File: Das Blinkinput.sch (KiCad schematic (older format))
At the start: 10 parts

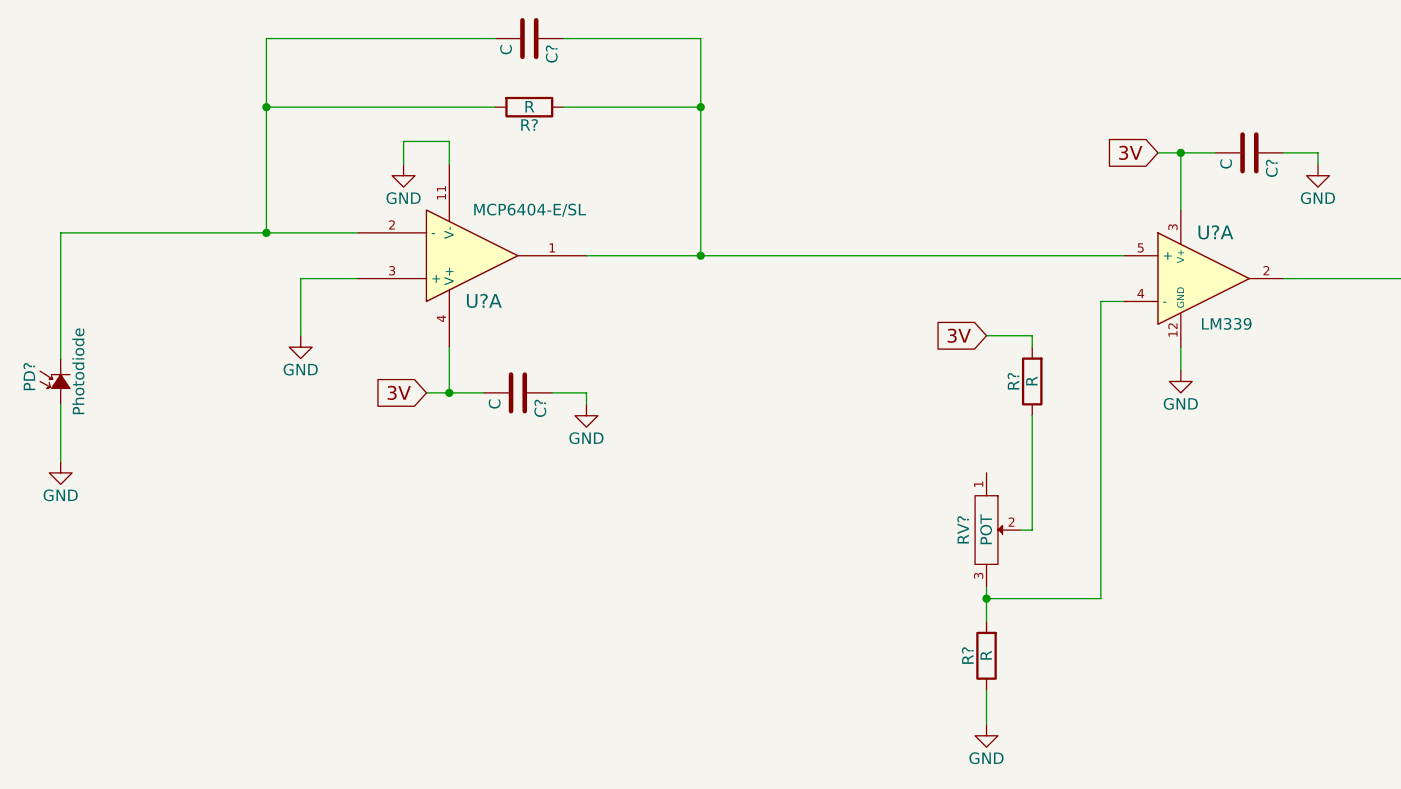
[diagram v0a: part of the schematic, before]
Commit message: Added part numbers and links to schematic
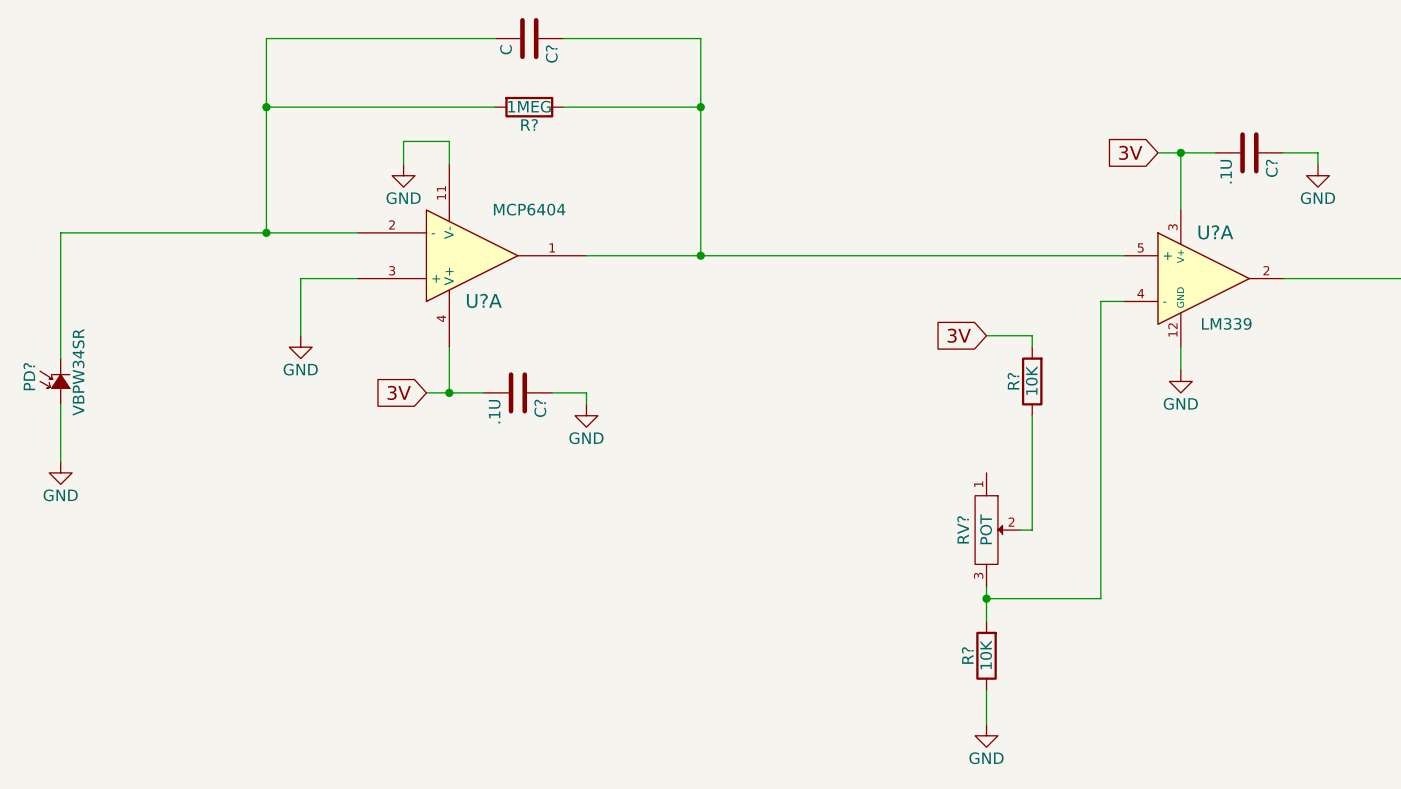
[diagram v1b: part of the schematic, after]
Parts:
- C? (x2): value C -> .1U
- PD?: value Photodiode -> VBPW34SR; Link (none) -> http://parts.io/detail/2942714/VBPW34SR; MPN (none) -> VBPW34SR
- R?: value R -> 1MEG; Link (none) -> http://parts.io/detail/880921/RC1206FR-071ML; MPN (none) -> RC1206FR-071ML
- R? (x2): value R -> 10K
- RV?: MPN (none) -> P090L-02F25BR10K
- U?: value MCP6404-E/SL -> MCP6404; Link (none) -> http://parts.io/detail/3584122/MCP6404-E%2FSL; MPN (none) -> MCP6404-E/SL
- U?: Link (none) -> http://parts.io/detail/916254/LM339DE4; MPN (none) -> LM339DE4
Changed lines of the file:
@@
 P 4350 2200
 F 0 "R?" V 4430 2200 50  0000 C CNN
-F 1 "R" V 4350 2200 50  0000 C CNN
+F 1 "1MEG" V 4350 2200 50  0000 C CNN
 F 2 "" V 4280 2200 30  0000 C CNN
 F 3 "" H 4350 2200 30  0000 C CNN
+F 4 "RC1206FR-071ML" V 4350 2200 60  0001 C CNN "MPN"
+F 5 "http://parts.io/detail/880921/RC1206FR-071ML" V 4350 2200 60  0001 C CNN "Link"
 	1    4350 2200
 	0    1    1    0
@@
 P 4100 2850
 F 0 "U?" H 4150 3050 60  0000 C CNN
-F 1 "MCP6404-E/SL" H 4350 2650 50  0000 C CNN
+F 1 "MCP6404" H 4350 2650 50  0000 C CNN
 F 2 "" H 4100 2850 60  0000 C CNN
 F 3 "" H 4100 2850 60  0000 C CNN
+F 4 "MCP6404-E/SL" H 4100 2850 60  0001 C CNN "MPN"
+F 5 "http://parts.io/detail/3584122/MCP6404-E%2FSL" H 4100 2850 60  0001 C CNN "Link"
 	1    4100 2850
 	1    0    0    1
@@
 P 2300 3400
 F 0 "PD?" H 2255 3535 50  0000 L CNN
-F 1 "Photodiode" H 2150 3320 50  0000 L CNN
+F 1 "VBPW34SR" H 2150 3320 50  0000 L CNN
 F 2 "" V 2300 3400 60  0000 C CNN
 F 3 "" V 2300 3400 60  0000 C CNN
+F 4 "VBPW34SR" H 2300 3400 60  0001 C CNN "MPN"
+F 5 "http://parts.io/detail/2942714/VBPW34SR" H 2300 3400 60  0001 C CNN "Link"
 	1    2300 3400
 	0    -1   -1   0
@@
 P 4300 3450
 F 0 "C?" H 4325 3550 50  0000 L CNN
-F 1 "C" H 4325 3350 50  0000 L CNN
+F 1 ".1U" H 4325 3350 50  0000 L CNN
 F 2 "" H 4338 3300 30  0000 C CNN
 F 3 "" H 4300 3450 60  0000 C CNN
@@
 F 2 "" H 7300 2950 60  0000 C CNN
 F 3 "" H 7300 2950 60  0000 C CNN
+F 4 "LM339DE4" H 7300 2950 60  0001 C CNN "MPN"
+F 5 "http://parts.io/detail/916254/LM339DE4" H 7300 2950 60  0001 C CNN "Link"
 	1    7300 2950
 	1    0    0    -1
@@
 P 6550 3400
 F 0 "R?" V 6630 3400 50  0000 C CNN
-F 1 "R" V 6550 3400 50  0000 C CNN
+F 1 "10K" V 6550 3400 50  0000 C CNN
 F 2 "" V 6480 3400 30  0000 C CNN
 F 3 "" H 6550 3400 30  0000 C CNN
@@
 P 6350 4600
 F 0 "R?" V 6430 4600 50  0000 C CNN
-F 1 "R" V 6350 4600 50  0000 C CNN
+F 1 "10K" V 6350 4600 50  0000 C CNN
 F 2 "" V 6280 4600 30  0000 C CNN
 F 3 "" H 6350 4600 30  0000 C CNN
@@
 F 2 "" H 6350 4050 60  0000 C CNN
 F 3 "" H 6350 4050 60  0000 C CNN
+F 4 "P090L-02F25BR10K" H 6350 4050 60  0001 C CNN "MPN"
 	1    6350 4050
 	0    1    1    0
@@
 P 7500 2400
 F 0 "C?" H 7525 2500 50  0000 L CNN
-F 1 "C" H 7525 2300 50  0000 L CNN
+F 1 ".1U" H 7525 2300 50  0000 L CNN
 F 2 "" H 7538 2250 30  0000 C CNN
 F 3 "" H 7500 2400 60  0000 C CNN

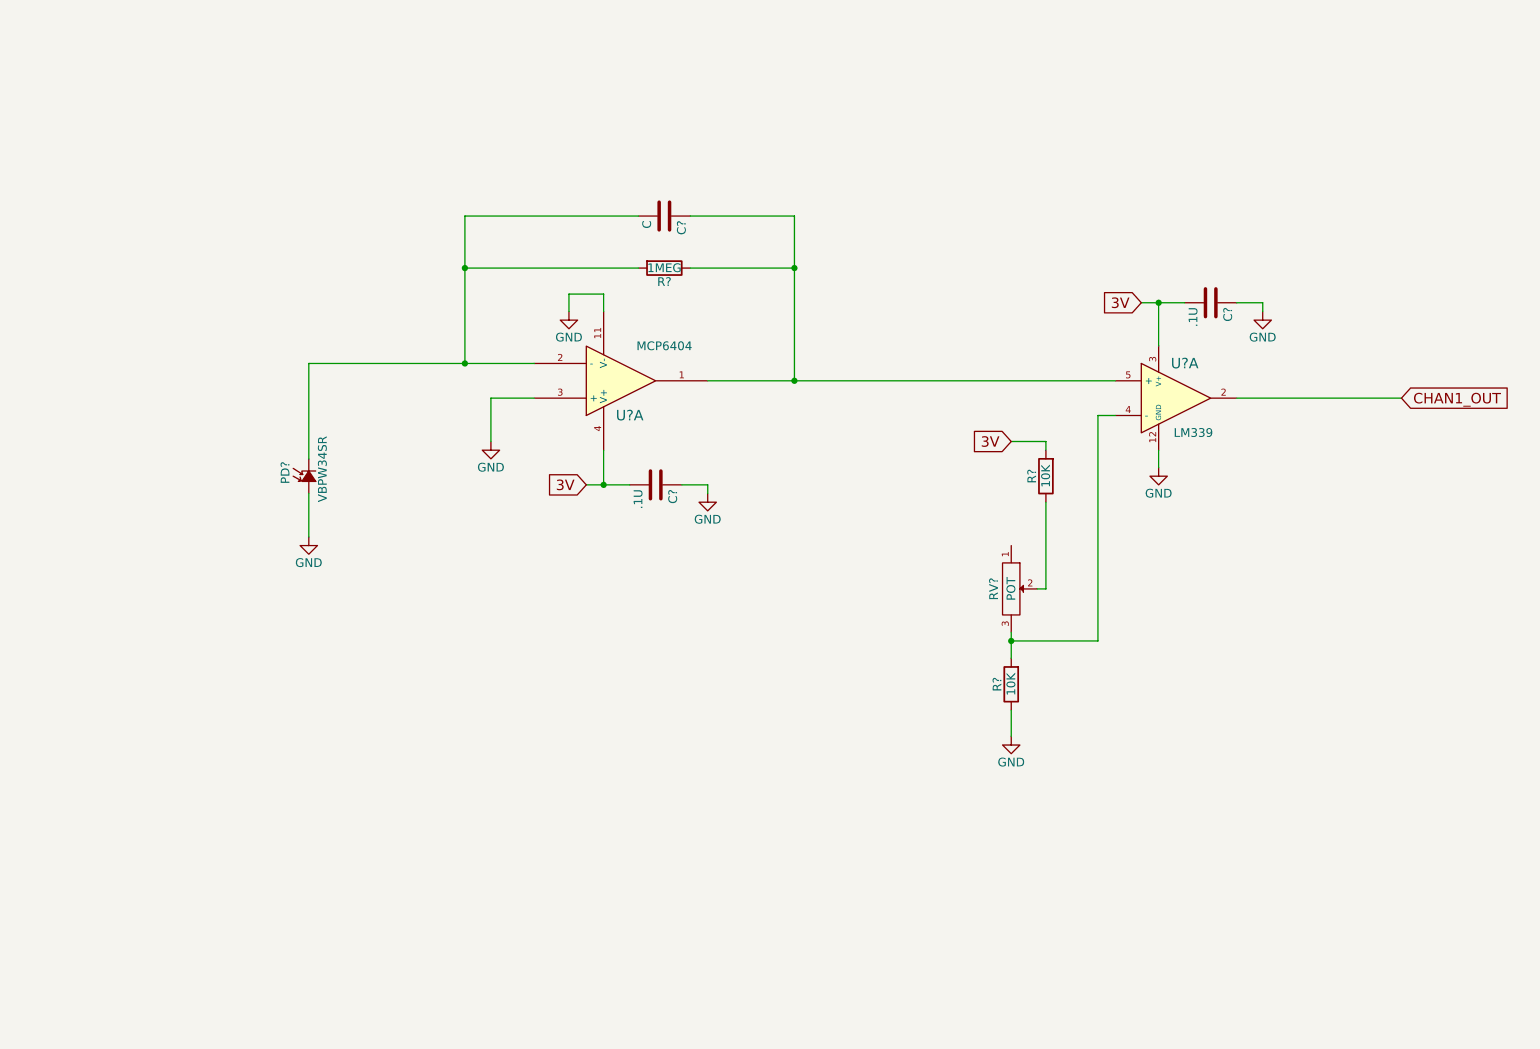
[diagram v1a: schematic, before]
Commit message: Channelizing the DB circuits
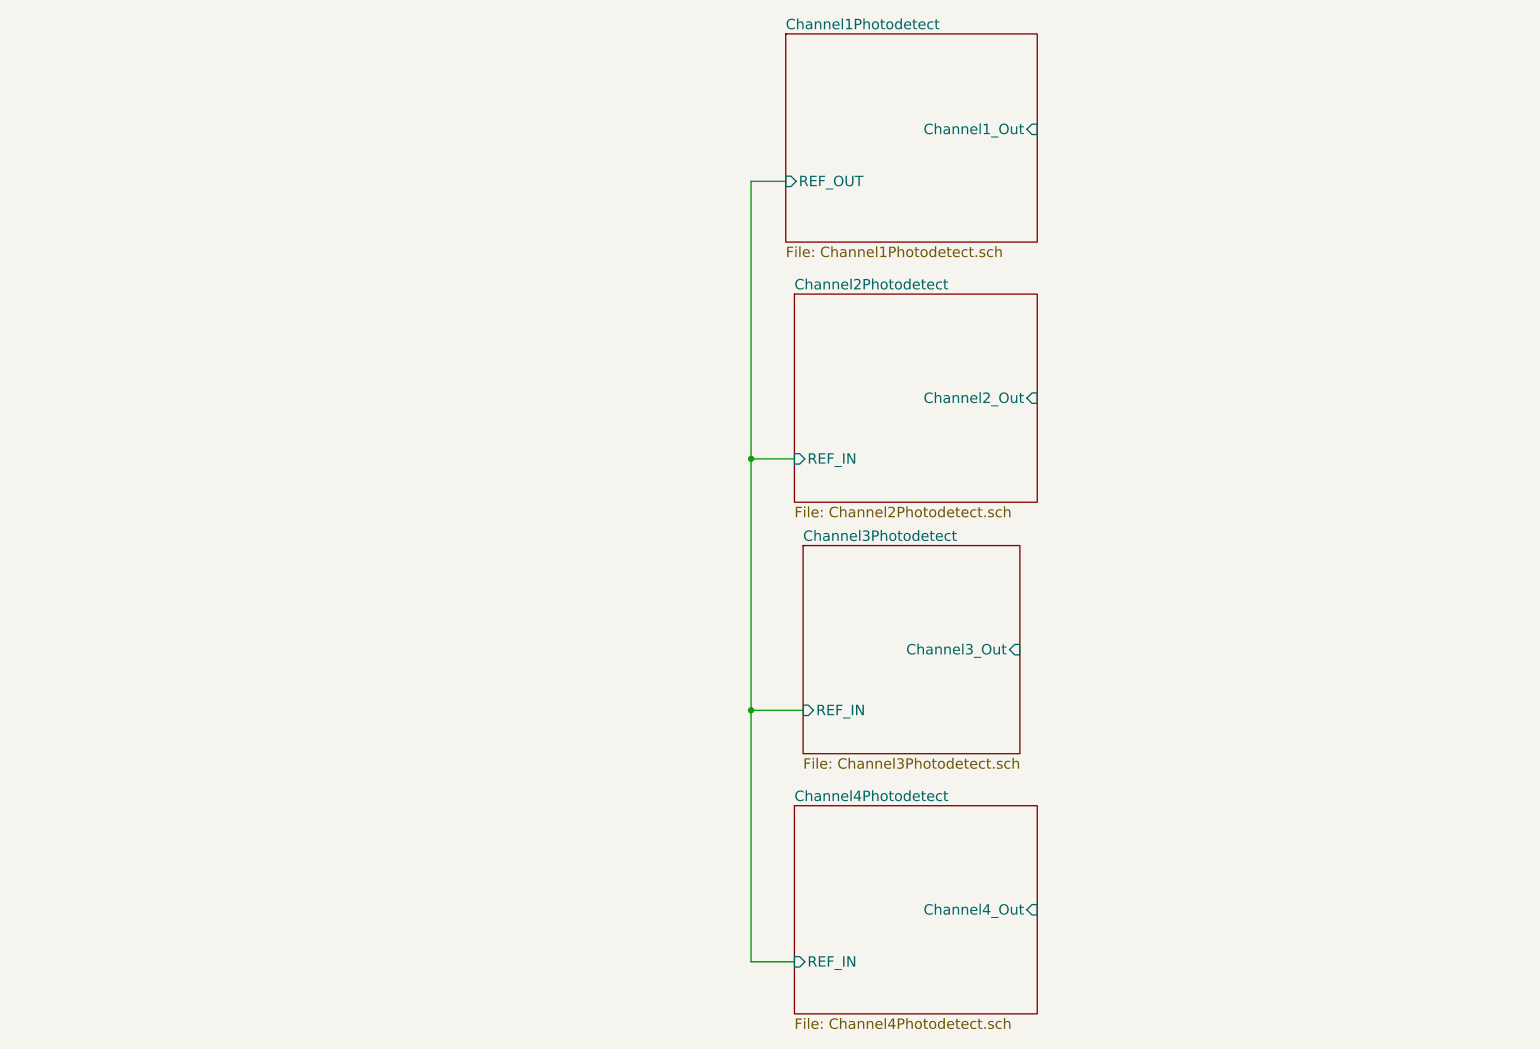
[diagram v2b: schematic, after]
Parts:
- removed C?: C, symbol C
- removed C? (x2): .1U, symbol C
- removed PD?: VBPW34SR, symbol Photodiode
- removed R?: 1MEG, symbol R
- removed R? (x2): 10K, symbol R
- removed RV?: POT, symbol POT
- removed U?: MCP6404, symbol MCP6404-E/SL
- removed U?: LM339, symbol LM339

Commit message: Added power regulator, VGND and test points
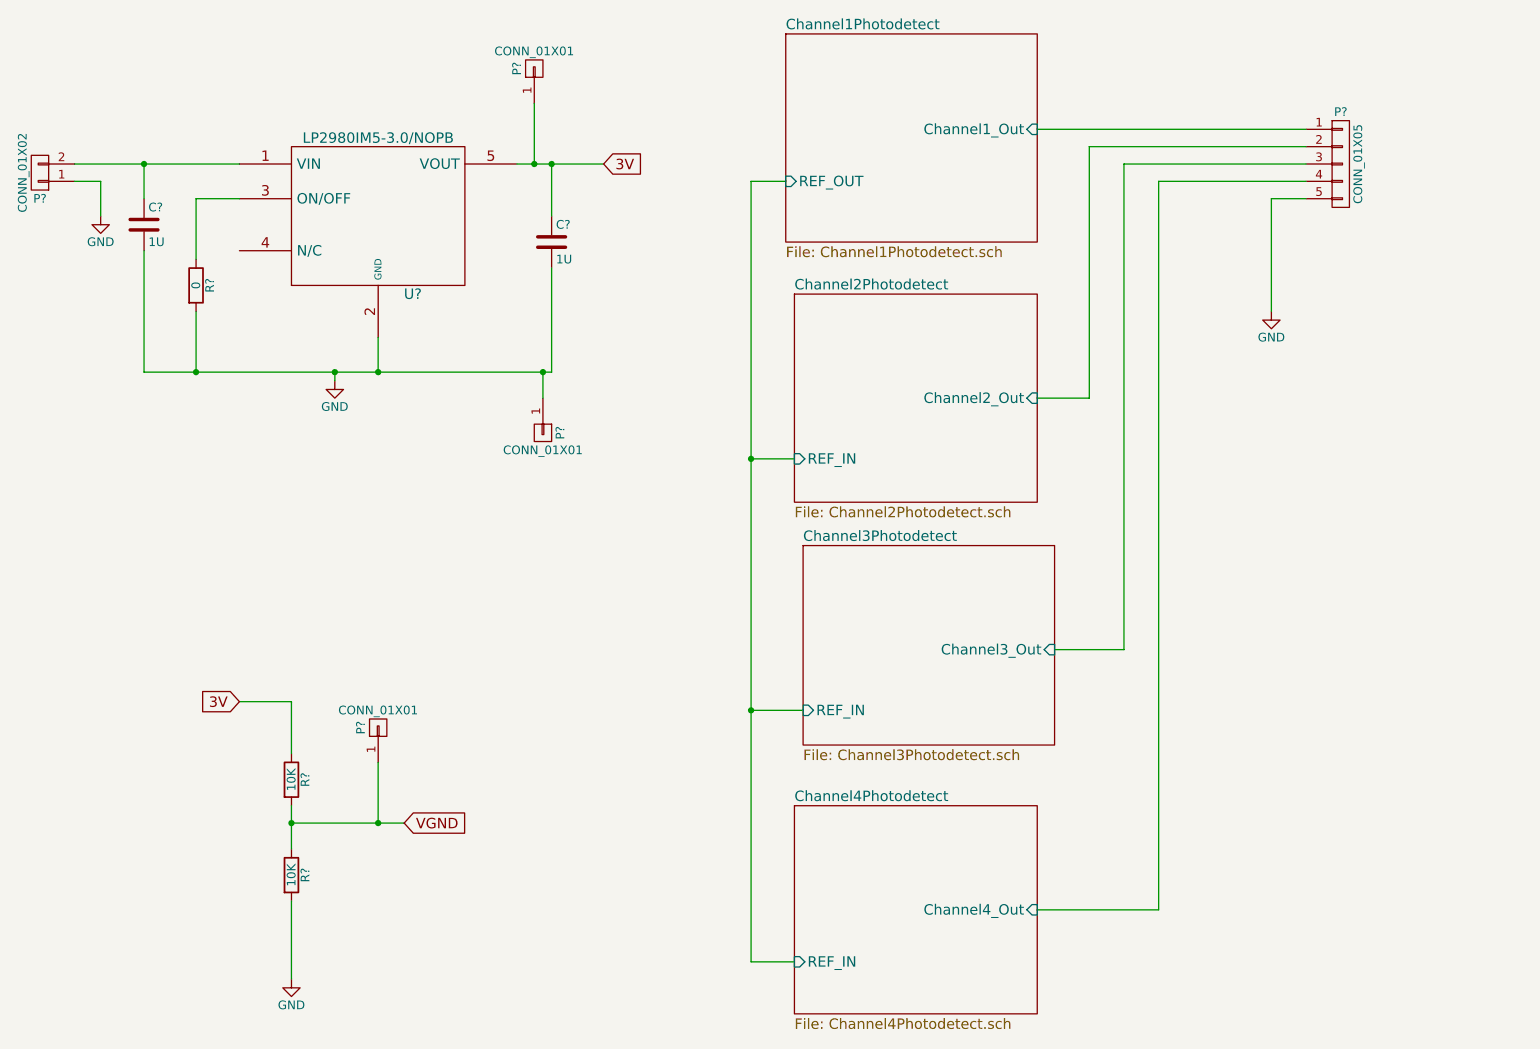
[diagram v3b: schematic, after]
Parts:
- added C? (x2): 1U, symbol C
- added P?: CONN_01X05, symbol CONN_01X05
- added P? (x3): CONN_01X01, symbol CONN_01X01
- added P?: CONN_01X02, symbol CONN_01X02
- added R?: 0, symbol R
- added R? (x2): 10K, symbol R
- added U?: LP2980IM5-3.0/NOPB, symbol LP2980IM5-3.0/NOPB
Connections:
- net Channel1Photodetect/Channel1_Out: now also P?.1 (P1)
- net Channel2Photodetect/Channel2_Out: now also P?.2 (P2)
- net Channel3Photodetect/Channel3_Out: now also P?.3 (P3)
- net Channel4Photodetect/Channel4_Out: now also P?.4 (P4)
- new net: C?.1, P?.2 (P2), U?.1 (VIN)
- new net: R?.1, U?.3 (ON/OFF)
- new net 3V: C?.1, P?.1 (P1), R?.1, U?.5 (VOUT)
- new net GND: C?.2, C?.2, P?.1 (P1), P?.1 (P1), P?.5 (P5), R?.2, R?.2, U?.2 (GND)
- new net VGND: P?.1 (P1), R?.1, R?.2

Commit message: Added libraries and imported components into the layout
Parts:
- gave numbers to parts that had none: 11
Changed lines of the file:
@@
 $EndSheet
 $Comp
-L CONN_01X05 P?
+L CONN_01X05 P105
 U 1 1 55562432
 P 8250 1600
-F 0 "P?" H 8250 1900 50  0000 C CNN
+F 0 "P105" H 8250 1900 50  0000 C CNN
 F 1 "CONN_01X05" V 8350 1600 50  0000 C CNN
 F 2 "" H 8250 1600 60  0000 C CNN
@@
 $EndComp
 $Comp
-L GND #PWR?
+L GND #PWR01
 U 1 1 5556319E
 P 7850 2450
-F 0 "#PWR?" H 7850 2200 50  0001 C CNN
+F 0 "#PWR01" H 7850 2200 50  0001 C CNN
 F 1 "GND" H 7850 2300 50  0000 C CNN
 F 2 "" H 7850 2450 60  0000 C CNN
@@
 $EndComp
 $Comp
-L CONN_01X02 P?
+L CONN_01X02 P101
 U 1 1 55563E64
 P 750 1650
-F 0 "P?" H 750 1800 50  0000 C CNN
+F 0 "P101" H 750 1800 50  0000 C CNN
 F 1 "CONN_01X02" V 850 1650 50  0000 C CNN
 F 2 "" H 750 1650 60  0000 C CNN
@@
 $EndComp
 $Comp
-L GND #PWR?
+L GND #PWR02
 U 1 1 55564325
 P 1100 1900
-F 0 "#PWR?" H 1100 1650 50  0001 C CNN
+F 0 "#PWR02" H 1100 1650 50  0001 C CNN
 F 1 "GND" H 1100 1750 50  0000 C CNN
 F 2 "" H 1100 1900 60  0000 C CNN
@@
 $EndComp
 $Comp
-L LP2980IM5-3.0/NOPB U?
+L LP2980IM5-3.0/NOPB U101
 U 1 1 55564A58
 P 2700 1900
-F 0 "U?" H 2900 1450 60  0000 C CNN
+F 0 "U101" H 2900 1450 60  0000 C CNN
 F 1 "LP2980IM5-3.0/NOPB" H 2700 2350 60  0000 C CNN
 F 2 "" H 2700 1900 60  0000 C CNN
@@
 $EndComp
 $Comp
-L C C?
+L C C101
 U 1 1 555651D9
 P 1350 1950
-F 0 "C?" H 1375 2050 50  0000 L CNN
+F 0 "C101" H 1375 2050 50  0000 L CNN
 F 1 "1U" H 1375 1850 50  0000 L CNN
 F 2 "" H 1388 1800 30  0000 C CNN
@@
 $EndComp
 $Comp
-L C C?
+L C C102
 U 1 1 55565240
 P 3700 2050
-F 0 "C?" H 3725 2150 50  0000 L CNN
+F 0 "C102" H 3725 2150 50  0000 L CNN
 F 1 "1U" H 3725 1950 50  0000 L CNN
 F 2 "" H 3738 1900 30  0000 C CNN
@@
 	3700 1600 3700 1900
 $Comp
-L R R?
+L R R101
 U 1 1 55566A0E
 P 1650 2300
-F 0 "R?" V 1730 2300 50  0000 C CNN
+F 0 "R101" V 1730 2300 50  0000 C CNN
 F 1 "0" V 1650 2300 50  0000 C CNN
 F 2 "" V 1580 2300 30  0000 C CNN
@@
 3V
 $Comp
-L R R?
+L R R102
 U 1 1 5556A99F
 P 2200 5150
-F 0 "R?" V 2280 5150 50  0000 C CNN
+F 0 "R102" V 2280 5150 50  0000 C CNN
 F 1 "10K" V 2200 5150 50  0000 C CNN
 F 2 "" V 2130 5150 30  0000 C CNN
@@
 $EndComp
 $Comp
-L R R?
+L R R103
 U 1 1 5556AA2C
 P 2200 5700
-F 0 "R?" V 2280 5700 50  0000 C CNN
+F 0 "R103" V 2280 5700 50  0000 C CNN
 F 1 "10K" V 2200 5700 50  0000 C CNN
 F 2 "" V 2130 5700 30  0000 C CNN
@@
 	2200 5850 2200 6300
 $Comp
-L GND #PWR?
+L GND #PWR03
 U 1 1 5556AB87
 P 2450 2850
-F 0 "#PWR?" H 2450 2600 50  0001 C CNN
+F 0 "#PWR03" H 2450 2600 50  0001 C CNN
 F 1 "GND" H 2450 2700 50  0000 C CNN
 F 2 "" H 2450 2850 60  0000 C CNN
@@
 Connection ~ 2450 2800
 $Comp
-L GND #PWR?
+L GND #PWR04
 U 1 1 5556B658
 P 2200 6300
-F 0 "#PWR?" H 2200 6050 50  0001 C CNN
+F 0 "#PWR04" H 2200 6050 50  0001 C CNN
 F 1 "GND" H 2200 6150 50  0000 C CNN
 F 2 "" H 2200 6300 60  0000 C CNN
@@
 VGND
 $Comp
-L CONN_01X01 P?
+L CONN_01X01 P103
 U 1 1 55563D09
 P 3600 1050
-F 0 "P?" H 3600 1150 50  0000 C CNN
+F 0 "P103" H 3600 1150 50  0000 C CNN
 F 1 "CONN_01X01" V 3700 1050 50  0000 C CNN
 F 2 "" H 3600 1050 60  0000 C CNN
@@
 Connection ~ 3600 1600
 $Comp
-L CONN_01X01 P?
+L CONN_01X01 P102
 U 1 1 555640A4
 P 2700 4850
-F 0 "P?" H 2700 4950 50  0000 C CNN
+F 0 "P102" H 2700 4950 50  0000 C CNN
 F 1 "CONN_01X01" V 2800 4850 50  0000 C CNN
 F 2 "" H 2700 4850 60  0000 C CNN
@@
 Connection ~ 2700 5400
 $Comp
-L CONN_01X01 P?
+L CONN_01X01 P104
 U 1 1 5556454C
 P 3650 3150
-F 0 "P?" H 3650 3250 50  0000 C CNN
+F 0 "P104" H 3650 3250 50  0000 C CNN
 F 1 "CONN_01X01" V 3750 3150 50  0000 C CNN
 F 2 "" H 3650 3150 60  0000 C CNN
